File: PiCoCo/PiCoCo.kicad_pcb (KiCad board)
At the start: 2 copper layers, 98 x 77.2 mm, 60 parts, among them P1 COCO-CART, Q2 2N7002, Q3 2N7002, Q4 2N7002, U1 Pico 2 / RP2350B-Plus-W, U10 SN74LVC245A, U11 SN74LVC245A, U12 SN74LVC245A, U13 SN74LVC245A, U14 AMS1117-3.3, U15 SN74LVC00A

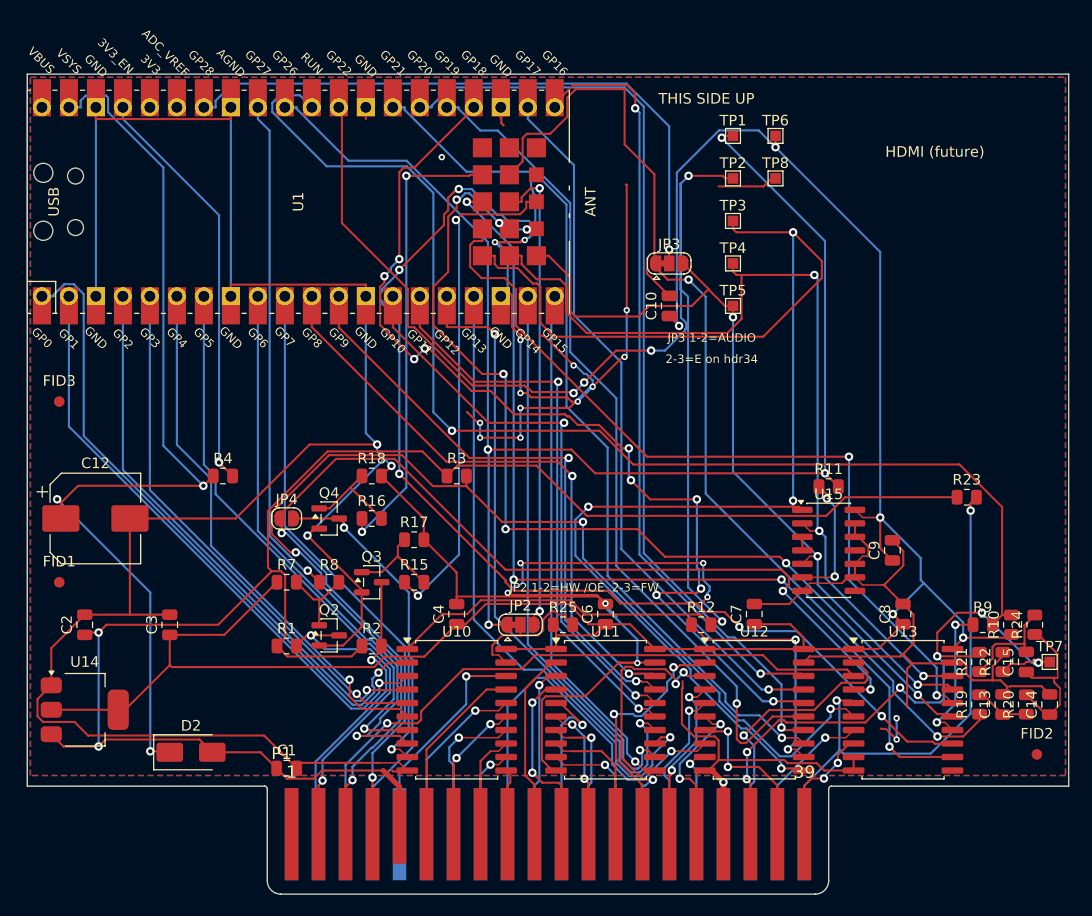
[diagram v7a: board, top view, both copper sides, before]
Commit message: kicad: hand-soldering pass — spaced audio cluster and FET stage, freed JP2/R25/R12/R11, legible refdes
- Audio chain + RUN pull-ups in two columns (x 190.3 / 194.9) at a 3.6 mm row pitch;
  FET stage (Q2-Q4 and resistors) on a 5 mm grid; R25/R12/R11/JP2/R3 moved out of
  the SOIC courtyards. No courtyard gap under 0.56 mm remains (decoupling caps by design).
- tools/tidy_refdes.py: every reference designator upright above (buffers: below)
  its courtyard; P1/fiducial labels hidden. Silk warnings 61 -> 33, overlaps 17 -> 1.
- Re-routed from scratch (Freerouting + finish_route); finish_route re-execs for the
  post-route phase and removes dangling items by DRC UUID.
- DRC --severity-all --schematic-parity: 0 errors, 0 unconnected, 0 parity.

Co-Authored-By: Claude Fable 5.1 <noreply@anthropic.com>
Claude-Session: https://claude.ai/code/session_013jbrP69zFzwzxjawTKy2c7
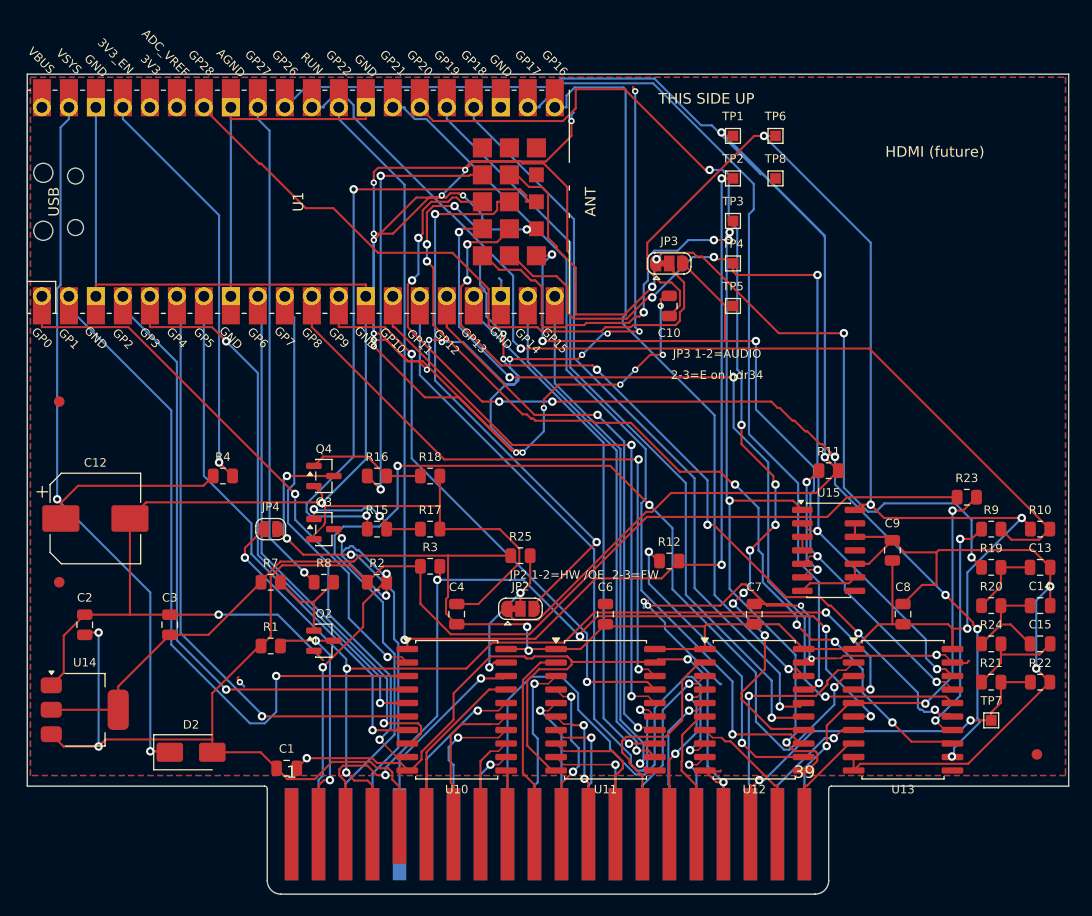
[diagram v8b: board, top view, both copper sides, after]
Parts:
- moved C13 13.4 mm to (194.9, 78.6), turned to 0 degrees
- moved R19 12.9 mm to (190.3, 78.6), turned to 0 degrees
- moved R20 9.87 mm to (190.3, 82.2), turned to 0 degrees
- moved R10 9.40 mm to (194.9, 75.0), turned to 0 degrees
- moved C14 9.34 mm to (194.9, 82.2), turned to 0 degrees
- moved R9 9.04 mm to (190.3, 75.0)
- moved R3 8.86 mm to (137.5, 78.5)
- moved TP7 7.78 mm to (190.3, 93.0)
- moved R25 7.63 mm to (146.0, 77.5)
- moved Q3 6.73 mm to (127.5, 75.0)
- moved R12 6.71 mm to (160.0, 78.0)
- moved R15 6.10 mm to (132.5, 75.0)
- moved R2 6.02 mm to (132.5, 80.0)
- moved R18 5.50 mm to (137.5, 70.0)
- moved R24 4.48 mm to (190.3, 85.8), turned to 0 degrees
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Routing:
- net GND: track 508.3 -> 662.6 mm, vias 26 -> 40
- net E_CART: track 59.9 -> 107.2 mm, vias 1 -> 3
- net CTS_BUF: track 133.6 -> 100.3 mm, vias 4 -> 6
- net RESET_CART: track 112.9 -> 84.8 mm, vias 4 -> 5
- net RW_BUF: track 149.3 -> 124.0 mm, vias 5 -> 3
- net A10_BUF: track 94.9 -> 70.7 mm, vias 10 -> 1
- net SND_CART: track 57.7 -> 36.5 mm, vias 6 -> 2
- net PICO_RUN: track 113.8 -> 96.6 mm
- net +5V: track 164.8 -> 147.7 mm
- net NMI_CART: track 27.8 -> 42.8 mm, vias 1 -> 4
- net SLENB_BUF: track 92.0 -> 77.5 mm
- net RW_CART: track 38.2 -> 52.2 mm
- net Q_CART: track 107.0 -> 93.1 mm, vias 4 -> 5
- net AUDIO_PWM: track 96.1 -> 82.8 mm, vias 2 -> 4
- net A9_BUF: track 67.9 -> 77.8 mm
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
